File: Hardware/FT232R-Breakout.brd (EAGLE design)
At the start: 30.5 x 20.3 mm, 20 parts, among them U1 FT232R

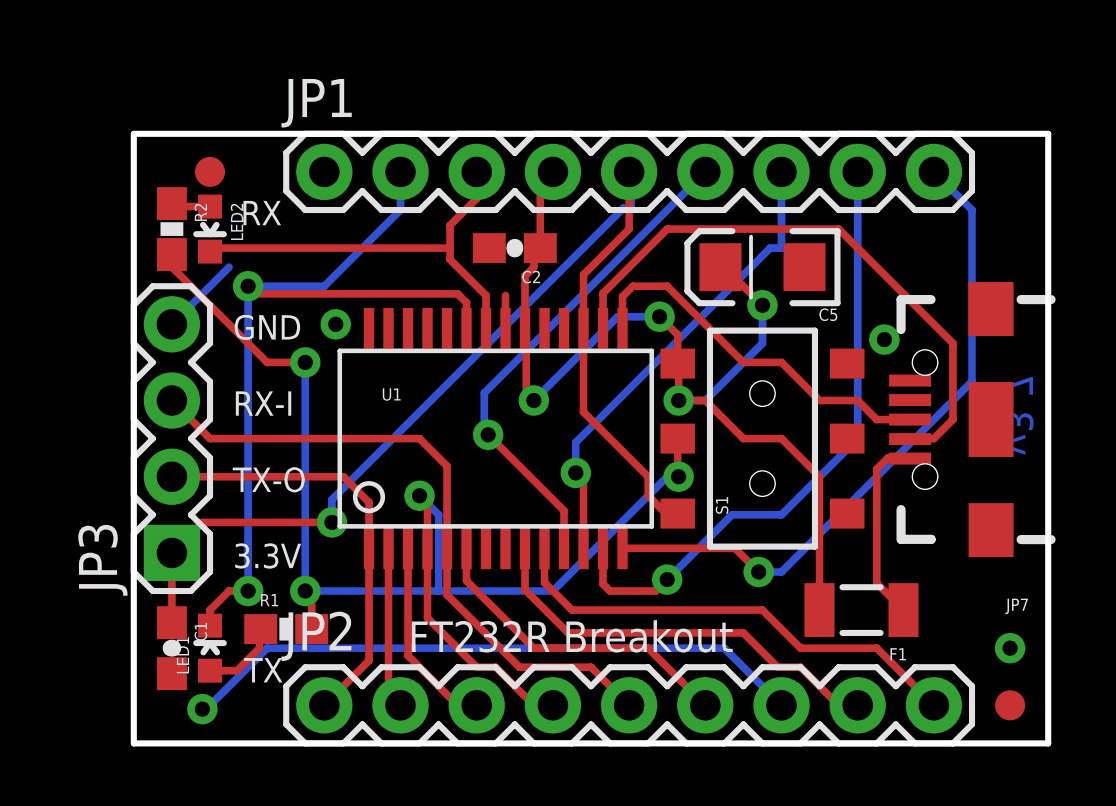
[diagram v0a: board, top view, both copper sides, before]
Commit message: Centering USB connector
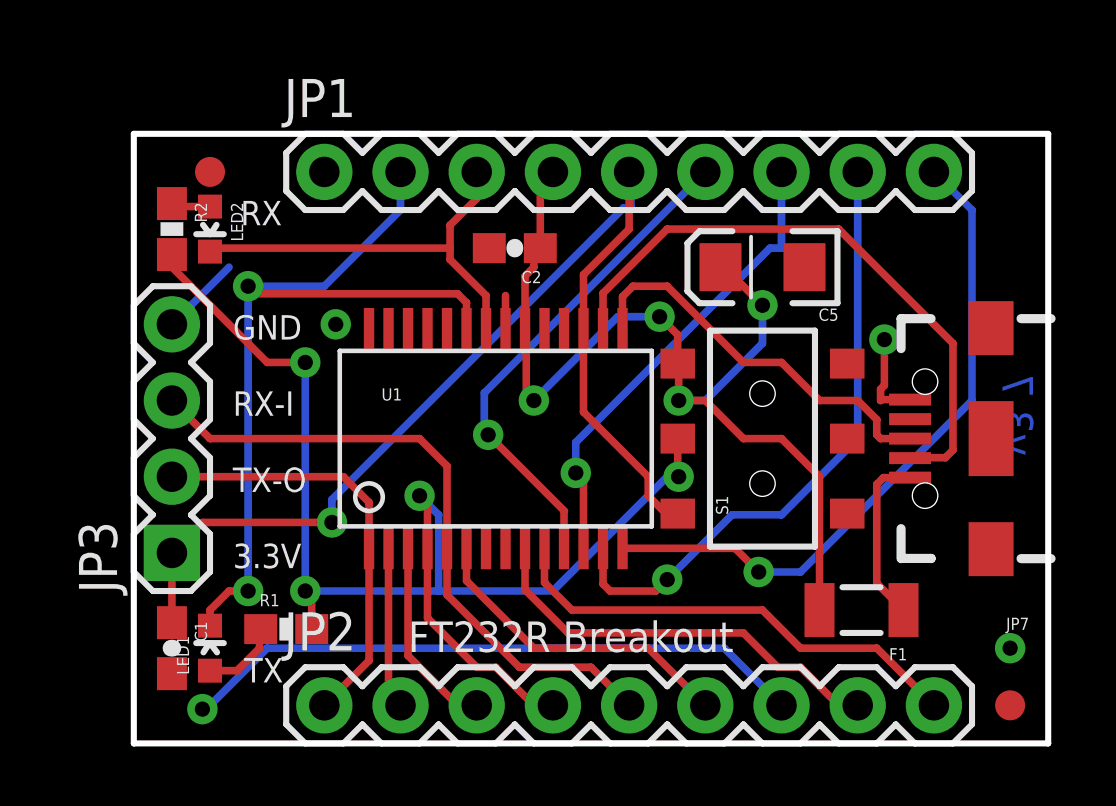
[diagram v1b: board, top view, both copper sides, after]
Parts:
- moved JP7 0.63 mm to (29.8, 11.4)
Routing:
- net GND: track 25.1 -> 28.2 mm
- net USB_D-: track 19.6 -> 20.4 mm
- net N$3: track 6.35 -> 5.76 mm
- net USB_D+: track 12.6 -> 13.2 mm

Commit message: Updating rev with recommendations from review
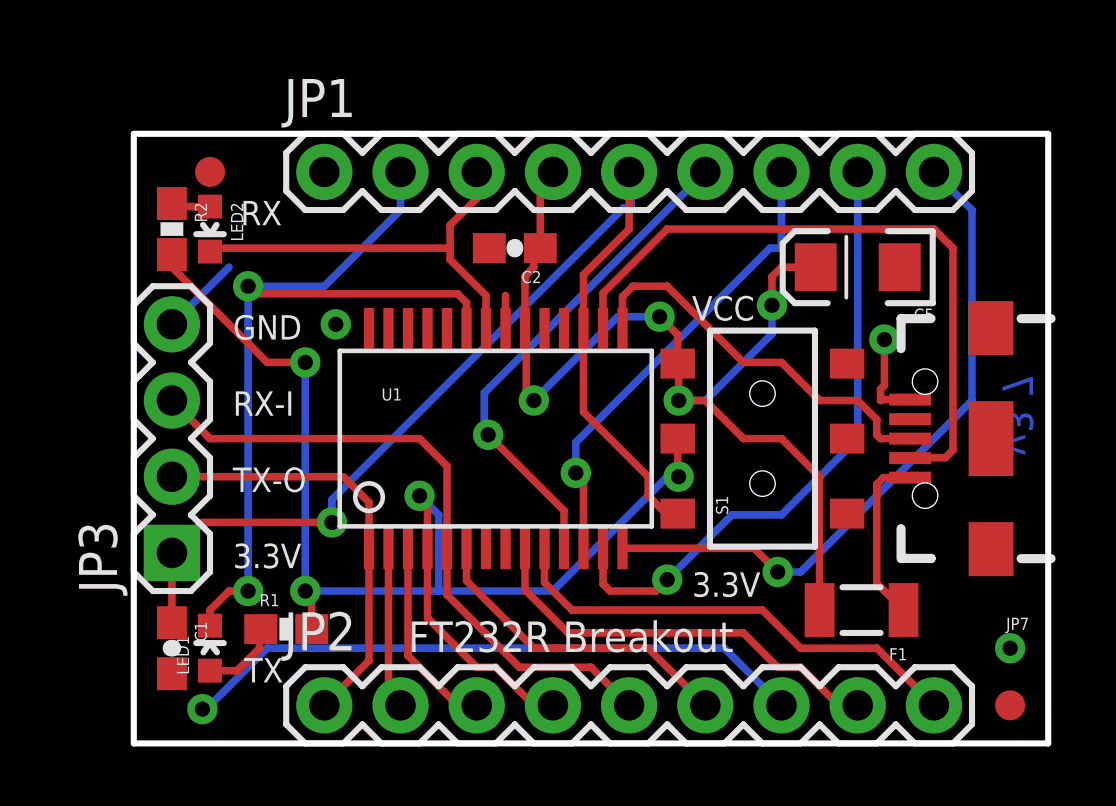
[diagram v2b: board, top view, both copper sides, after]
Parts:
- moved C5 3.17 mm to (25.4, 17.1)
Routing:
- net USB_D-: track 20.4 -> 22.3 mm
- net VCC: track 33.5 -> 34.3 mm
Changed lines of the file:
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@@
 <setting verticaltext="up"/>
 </settings>
-<grid distance="0.05" unitdist="inch" unit="inch" style="lines" multiple="1" display="yes" altdistance="0.005" altunitdist="inch" altunit="inch"/>
+<grid distance="0.0125" unitdist="inch" unit="inch" style="lines" multiple="1" display="yes" altdistance="0.005" altunitdist="inch" altunit="inch"/>
 <layers>
 <layer number="1" name="Top" color="4" fill="1" visible="yes" active="yes"/>
@@
 <text x="4.572" y="14.732" size="0.8128" layer="21" font="vector" ratio="15">GND</text>
 <text x="10.414" y="4.318" size="1.016" layer="21" font="vector" ratio="15">FT232R Breakout</text>
-<text x="15.875" y="19.177" size="1.4224" layer="22" font="vector" ratio="15" rot="MR270">VCC</text>
-<text x="18.415" y="19.177" size="1.4224" layer="22" font="vector" ratio="15" rot="MR270">V3.3</text>
-<text x="28.575" y="19.177" size="1.4224" layer="22" font="vector" ratio="15" rot="MR270">PWREN</text>
-<text x="26.035" y="19.177" size="1.4224" layer="22" font="vector" ratio="15" rot="MR270">TXDEN</text>
-<text x="23.495" y="19.177" size="1.4224" layer="22" font="vector" ratio="15" rot="MR270">SLEEP</text>
-<text x="13.335" y="19.177" size="1.4224" layer="22" font="vector" ratio="15" rot="MR270">RXLED</text>
-<text x="10.795" y="19.177" size="1.4224" layer="22" font="vector" ratio="15" rot="MR270">TXLED</text>
-<text x="14.478" y="4.191" size="1.4224" layer="22" font="vector" ratio="15" rot="MR90">VCCIO</text>
-<text x="20.955" y="19.177" size="1.4224" layer="22" font="vector" ratio="15" rot="MR270">CTS</text>
-<text x="27.178" y="4.191" size="1.4224" layer="22" font="vector" ratio="15" rot="MR90">DCD</text>
-<text x="24.638" y="4.191" size="1.4224" layer="22" font="vector" ratio="15" rot="MR90">DSR</text>
-<text x="19.685" y="4.191" size="1.4224" layer="22" font="vector" ratio="15" rot="MR90">RI</text>
-<text x="11.938" y="4.191" size="1.4224" layer="22" font="vector" ratio="15" rot="MR90">RTS</text>
-<text x="9.525" y="4.191" size="1.4224" layer="22" font="vector" ratio="15" rot="MR90">DTR</text>
-<text x="17.018" y="4.191" size="1.4224" layer="22" font="vector" ratio="15" rot="MR90">RXD</text>
-<text x="6.858" y="4.191" size="1.4224" layer="22" font="vector" ratio="15" rot="MR90">TXD</text>
-<text x="22.098" y="4.191" size="1.4224" layer="22" font="vector" ratio="15" rot="MR90">GND</text>
-<text x="8.255" y="19.177" size="1.4224" layer="22" font="vector" ratio="15" rot="MR270">GND</text>
+<text x="15.875" y="19.177" size="1.016" layer="22" font="vector" ratio="15" rot="MR270">VCC</text>
+<text x="18.415" y="19.177" size="1.016" layer="22" font="vector" ratio="15" rot="MR270">V3.3</text>
+<text x="28.575" y="19.177" size="1.016" layer="22" font="vector" ratio="15" rot="MR270">PWREN</text>
+<text x="26.035" y="19.177" size="1.016" layer="22" font="vector" ratio="15" rot="MR270">TXDEN</text>
+<text x="23.495" y="19.177" size="1.016" layer="22" font="vector" ratio="15" rot="MR270">SLEEP</text>
+<text x="13.335" y="19.177" size="1.016" layer="22" font="vector" ratio="15" rot="MR270">RXLED</text>
+<text x="10.795" y="19.177" size="1.016" layer="22" font="vector" ratio="15" rot="MR270">TXLED</text>
+<text x="14.478" y="4.191" size="1.016" layer="22" font="vector" ratio="15" rot="MR90">VCCIO</text>
+<text x="20.955" y="19.177" size="1.016" layer="22" font="vector" ratio="15" rot="MR270">CTS</text>
+<text x="27.178" y="4.191" size="1.016" layer="22" font="vector" ratio="15" rot="MR90">DCD</text>
+<text x="24.638" y="4.191" size="1.016" layer="22" font="vector" ratio="15" rot="MR90">DSR</text>
+<text x="19.685" y="4.191" size="1.016" layer="22" font="vector" ratio="15" rot="MR90">RI</text>
+<text x="11.938" y="4.191" size="1.016" layer="22" font="vector" ratio="15" rot="MR90">RTS</text>
+<text x="9.525" y="4.191" size="1.016" layer="22" font="vector" ratio="15" rot="MR90">DTR</text>
+<text x="17.018" y="4.191" size="1.016" layer="22" font="vector" ratio="15" rot="MR90">RXD</text>
+<text x="6.858" y="4.191" size="1.016" layer="22" font="vector" ratio="15" rot="MR90">TXD</text>
+<text x="22.098" y="4.191" size="1.016" layer="22" font="vector" ratio="15" rot="MR90">GND</text>
+<text x="8.255" y="19.177" size="1.016" layer="22" font="vector" ratio="15" rot="MR270">GND</text>
 <text x="4.826" y="18.542" size="0.8128" layer="21" font="vector" ratio="15">RX</text>
 <text x="4.953" y="3.302" size="0.8128" layer="21" font="vector" ratio="15">TX</text>
@@
 <text x="30.48" y="-8.89" size="1.778" layer="51" font="vector" ratio="15">Nathan Seidle</text>
 <text x="29.21" y="-11.43" size="1.778" layer="51" font="vector" ratio="15">Toni Klopfenstein</text>
+<text x="19.8755" y="6.1595" size="0.8128" layer="21" font="vector" ratio="15">3.3V</text>
+<text x="19.8755" y="15.367" size="0.8128" layer="21" font="vector" ratio="15">VCC</text>
 </plain>
 <attributes>
@@
 <attribute name="PROD_ID" value="CAP-00810" x="13.97" y="17.78" size="1.778" layer="27" rot="R180" display="off"/>
 </element>
-<element name="C5" library="SparkFun-Capacitors" package="EIA3216" value="10uF" x="22.225" y="17.145" smashed="yes" rot="R180">
-<attribute name="NAME" x="24.765" y="15.764" size="0.4064" layer="25" rot="R180"/>
-<attribute name="VALUE" value="10uF" x="22.706" y="16.194" size="0.4064" layer="27" rot="R180"/>
-<attribute name="PROD_ID" value="CAP-00811" x="22.225" y="17.145" size="1.778" layer="27" rot="R180" display="off"/>
+<element name="C5" library="SparkFun-Capacitors" package="EIA3216" value="10uF" x="25.4" y="17.145" smashed="yes" rot="R180">
+<attribute name="NAME" x="27.94" y="15.764" size="0.4064" layer="25" rot="R180"/>
+<attribute name="VALUE" value="10uF" x="25.881" y="16.194" size="0.4064" layer="27" rot="R180"/>
+<attribute name="PROD_ID" value="CAP-00811" x="25.4" y="17.145" size="1.778" layer="27" rot="R180" display="off"/>
 </element>
 <element name="C1" library="SparkFun-Capacitors" package="0603-CAP" value="0.1uF" x="2.54" y="4.445" smashed="yes" rot="R270">
@@
 <contactref element="U1" pad="16"/>
 <contactref element="JP7" pad="D-1"/>
-<wire x1="28.575" y1="11.049" x2="28.575" y2="14.605" width="0.254" layer="1"/>
+<wire x1="28.575" y1="11.049" x2="28.575" y2="17.78" width="0.254" layer="1"/>
 <wire x1="16.91" y1="15.086" x2="16.91" y2="16.275" width="0.254" layer="1"/>
 <wire x1="16.91" y1="16.275" x2="19.05" y2="18.415" width="0.254" layer="1"/>
-<wire x1="19.05" y1="18.415" x2="24.765" y2="18.415" width="0.254" layer="1"/>
-<wire x1="24.765" y1="18.415" x2="28.575" y2="14.605" width="0.254" layer="1"/>
+<wire x1="19.05" y1="18.415" x2="27.94" y2="18.415" width="0.254" layer="1"/>
 <wire x1="28.575" y1="11.049" x2="28.321" y2="10.795" width="0.254" layer="1"/>
 <wire x1="28.321" y1="10.795" x2="27.16" y2="10.795" width="0.254" layer="1"/>
 <wire x1="27.16" y1="10.795" x2="27.145" y2="10.78" width="0.254" layer="1"/>
+<wire x1="28.575" y1="17.78" x2="27.94" y2="18.415" width="0.254" layer="1"/>
 </signal>
 <signal name="USB_D+">
@@
 <wire x1="14.82" y1="17.78" x2="14.82" y2="19.9" width="0.254" layer="1"/>
 <wire x1="14.82" y1="19.9" x2="15.24" y2="20.32" width="0.254" layer="1"/>
-<wire x1="20.825" y1="17.145" x2="20.955" y2="17.145" width="0.254" layer="1"/>
-<wire x1="20.955" y1="17.145" x2="22.225" y2="15.875" width="0.254" layer="1"/>
-<via x="22.225" y="15.875" extent="1-16" drill="0.508"/>
+<via x="22.5425" y="15.875" extent="1-16" drill="0.508"/>
 <via x="19.431" y="12.7" extent="1-16" drill="0.508"/>
 <wire x1="22.86" y1="11.43" x2="21.59" y2="11.43" width="0.254" layer="1"/>
@@
 <wire x1="19.431" y1="12.7" x2="19.431" y2="13.899" width="0.254" layer="1"/>
 <wire x1="19.431" y1="13.899" x2="19.4" y2="13.93" width="0.254" layer="1"/>
-<wire x1="22.225" y1="15.875" x2="22.225" y2="14.605" width="0.254" layer="16"/>
-<wire x1="22.225" y1="14.605" x2="20.32" y2="12.7" width="0.254" layer="16"/>
+<wire x1="22.5425" y1="14.9225" x2="20.32" y2="12.7" width="0.254" layer="16"/>
 <wire x1="20.32" y1="12.7" x2="19.431" y2="12.7" width="0.254" layer="16"/>
 <via x="18.796" y="15.494" extent="1-16" drill="0.508"/>
@@
 <wire x1="17.399" y1="15.494" x2="14.605" y2="12.7" width="0.254" layer="16"/>
 <wire x1="18.796" y1="15.494" x2="17.399" y2="15.494" width="0.254" layer="16"/>
+<wire x1="22.86" y1="17.145" x2="24" y2="17.145" width="0.254" layer="1"/>
+<wire x1="22.86" y1="17.145" x2="22.5425" y2="16.8275" width="0.254" layer="1"/>
+<wire x1="22.5425" y1="16.8275" x2="22.5425" y2="15.875" width="0.254" layer="1"/>
+<wire x1="22.5425" y1="14.9225" x2="22.5425" y2="15.875" width="0.254" layer="16"/>
 </signal>
 <signal name="TXD">
@@
 <contactref element="U1" pad="14"/>
 <contactref element="JP1" pad="9"/>
-<via x="22.098" y="6.985" extent="1-16" drill="0.508"/>
+<via x="22.733" y="6.985" extent="1-16" drill="0.508"/>
 <wire x1="29.21" y1="12.7" x2="29.21" y2="19.05" width="0.254" layer="16"/>
 <wire x1="29.21" y1="19.05" x2="27.94" y2="20.32" width="0.254" layer="16"/>
-<wire x1="17.56" y1="7.774" x2="21.309" y2="7.774" width="0.254" layer="1"/>
-<wire x1="22.098" y1="6.985" x2="23.495" y2="6.985" width="0.254" layer="16"/>
-<wire x1="22.098" y1="6.985" x2="21.309" y2="7.774" width="0.254" layer="1"/>
+<wire x1="17.56" y1="7.774" x2="21.944" y2="7.774" width="0.254" layer="1"/>
 <wire x1="29.21" y1="12.7" x2="23.495" y2="6.985" width="0.254" layer="16"/>
+<wire x1="21.944" y1="7.774" x2="22.733" y2="6.985" width="0.254" layer="1"/>
+<wire x1="23.495" y1="6.985" x2="22.733" y2="6.985" width="0.254" layer="16"/>
 </signal>
 <signal name="TXDEN">
@@
 </signal>
 </signals>
+<errors>
+</errors>
 </board>
 </drawing>
